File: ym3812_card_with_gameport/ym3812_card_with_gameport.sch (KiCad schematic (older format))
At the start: 79 parts, among them IC1 74LS138, IC11 NE558, IC12 74HCT02, IC13 74LS74, IC18 74LS244, IC2 74LS138, IC3 74LS138, IC4 74LS245, IC6 YM3812, IC7 Y3014B, IC8 LM324, IC9 TDA7233, J1 Bus_ISA_8bit

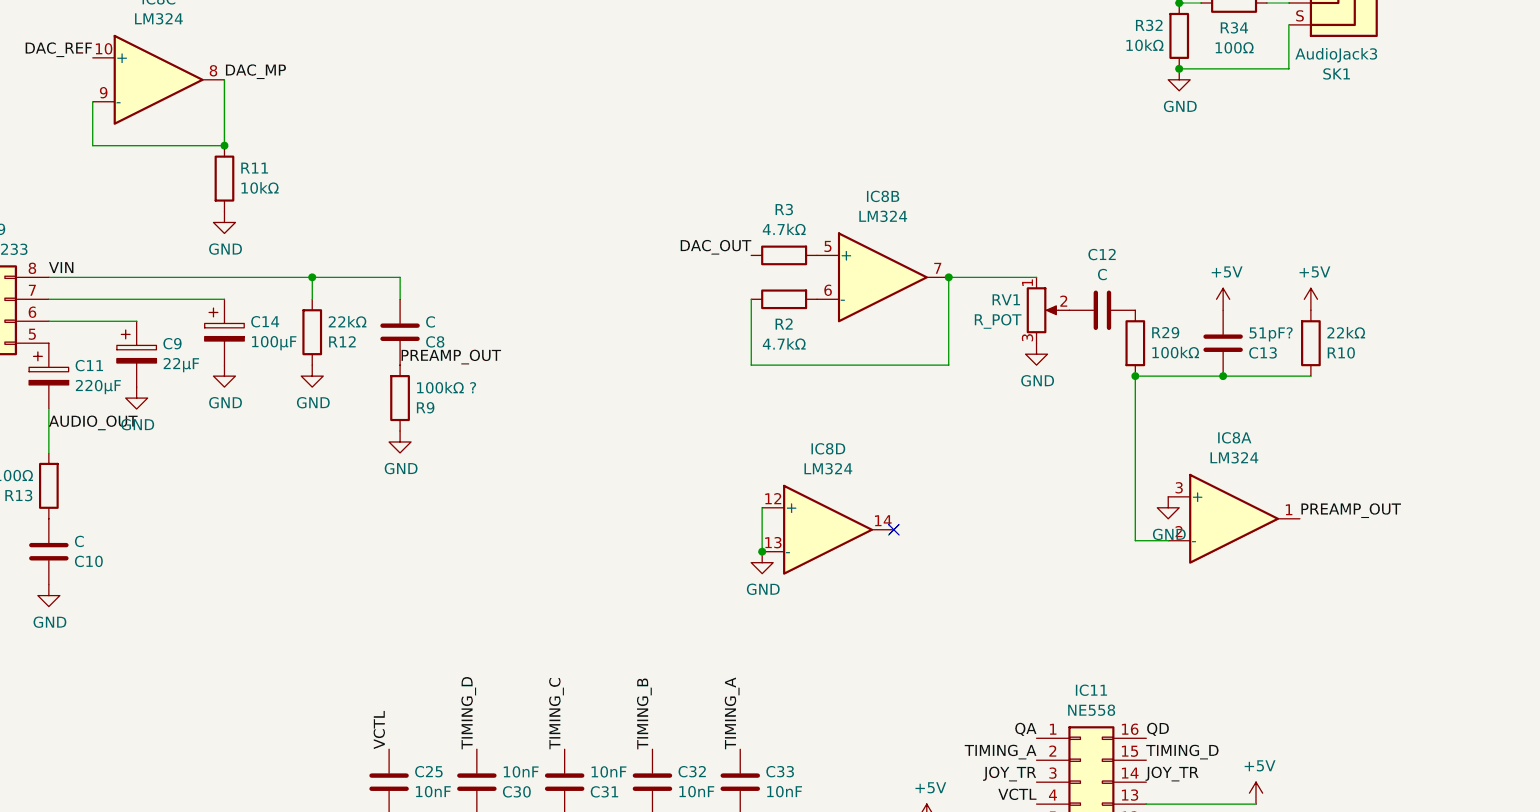
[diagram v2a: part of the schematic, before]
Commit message: corrections and some new traces
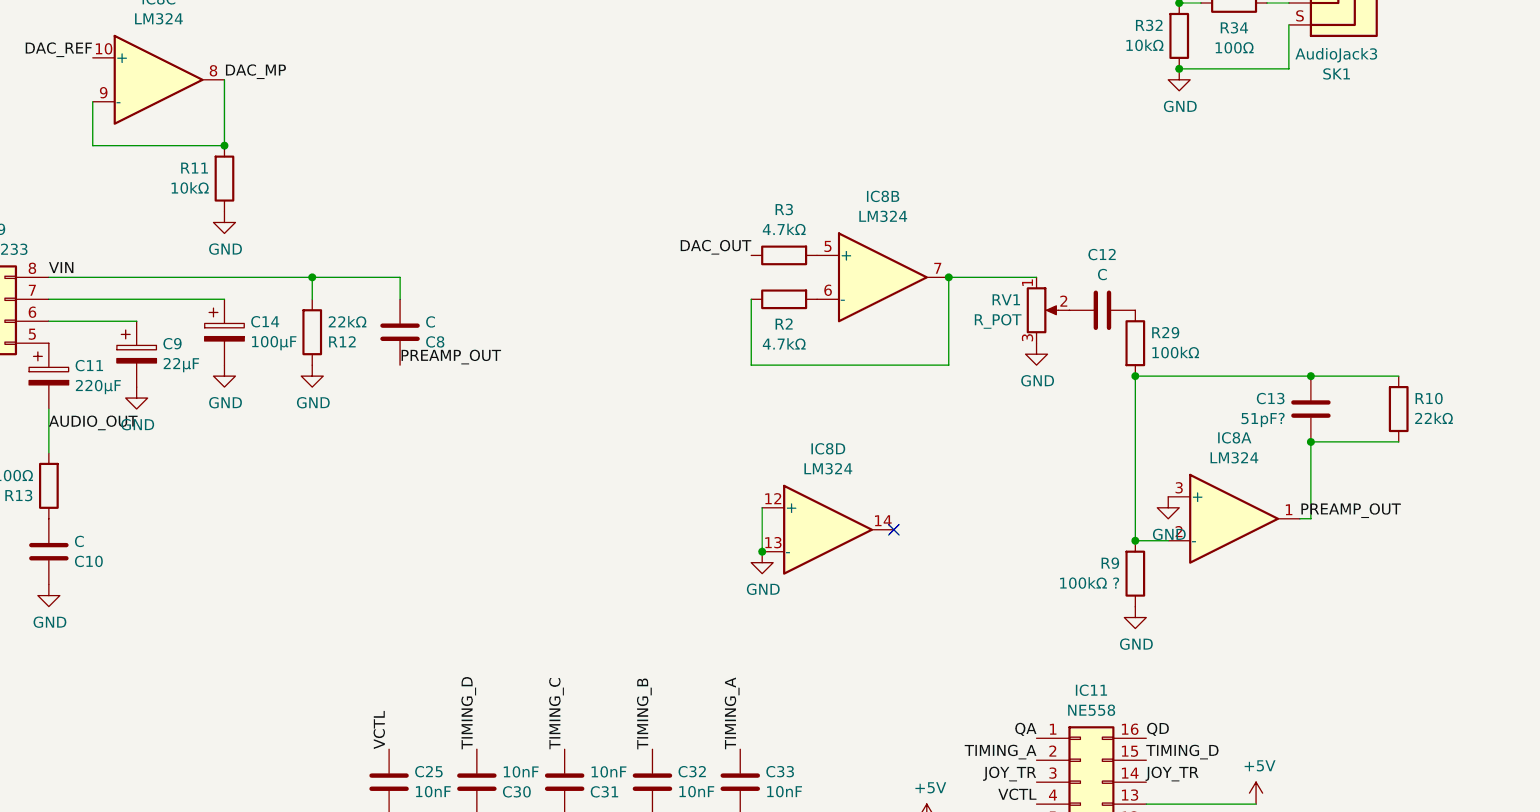
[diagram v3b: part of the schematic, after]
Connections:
- net +5V: no longer C13.2, R10.2
- net DAC_MP: now also R11.2; no longer R11.1
- net GND: now also R11.1; no longer R11.2
- net PREAMP_OUT: now also C13.1, R10.1; no longer R9.2
- net at IC8.2 (-), R29.2: now also C13.2, R10.2, R9.2; no longer C13.1, R10.1
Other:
- moved on the sheet: C13, R10, R9
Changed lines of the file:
@@
 EESchema Schematic File Version 4
-LIBS:ym3812_card_with_gameport-cache
 EELAYER 30 0
 EELAYER END
@@
 U 1 1 5D98CD88
 P 10200 2350
-F 0 "R11" H 10270 2396 50  0000 L CNN
-F 1 "10kΩ" H 10270 2305 50  0000 L CNN
+F 0 "R11" H 10131 2304 50  0000 R CNN
+F 1 "10kΩ" H 10131 2395 50  0000 R CNN
 F 2 "Resistor_SMD:R_1206_3216Metric" V 10130 2350 50  0001 C CNN
 F 3 "~" H 10200 2350 50  0001 C CNN
 	1    10200 2350
-	1    0    0    -1
+	1    0    0    1
 $EndComp
 $Comp
@@
 $EndComp
 $Comp
-L Device:R R10
-U 1 1 5D98D108
-P 15150 3100
-F 0 "R10" H 15220 3146 50  0000 L CNN
-F 1 "22kΩ" H 15220 3055 50  0000 L CNN
-F 2 "Resistor_SMD:R_1206_3216Metric" V 15080 3100 50  0001 C CNN
-F 3 "~" H 15150 3100 50  0001 C CNN
-	1    15150 3100
-	1    0    0    1
-$EndComp
-$Comp
 L Device:R R33
 U 1 1 5D98D9BF
@@
 L Device:R R9
 U 1 1 5D98DBBF
-P 11000 3350
-F 0 "R9" H 11070 3396 50  0000 L CNN
-F 1 "100kΩ ?" H 11070 3305 50  0000 L CNN
-F 2 "Resistor_SMD:R_1206_3216Metric" V 10930 3350 50  0001 C CNN
-F 3 "~" H 11000 3350 50  0001 C CNN
-	1    11000 3350
+P 14350 4150
+F 0 "R9" H 14281 4104 50  0000 R CNN
+F 1 "100kΩ ?" H 14281 4195 50  0000 R CNN
+F 2 "Resistor_SMD:R_1206_3216Metric" V 14280 4150 50  0001 C CNN
+F 3 "~" H 14350 4150 50  0001 C CNN
+	1    14350 4150
 	1    0    0    1
 $EndComp
@@
 $EndComp
 $Comp
-L Device:C C13
-U 1 1 5D9C6C30
-P 14750 3100
-F 0 "C13" H 14865 3146 50  0000 L CNN
-F 1 "51pF?" H 14865 3055 50  0000 L CNN
-F 2 "Capacitor_SMD:C_1206_3216Metric" H 14788 2950 50  0001 C CNN
-F 3 "~" H 14750 3100 50  0001 C CNN
-	1    14750 3100
-	1    0    0    1
-$EndComp
-$Comp
 L Device:C C34
 U 1 1 5D9C6E25
@@
 L power:GND #PWR0130
 U 1 1 5DB4EF8C
-P 11000 3500
-F 0 "#PWR0130" H 11000 3250 50  0001 C CNN
-F 1 "GND" H 11005 3327 50  0000 C CNN
-F 2 "" H 11000 3500 50  0001 C CNN
-F 3 "" H 11000 3500 50  0001 C CNN
-	1    11000 3500
+P 14350 4300
+F 0 "#PWR0130" H 14350 4050 50  0001 C CNN
+F 1 "GND" H 14355 4127 50  0000 C CNN
+F 2 "" H 14350 4300 50  0001 C CNN
+F 3 "" H 14350 4300 50  0001 C CNN
+	1    14350 4300
 	1    0    0    -1
 $EndComp
@@
 Text Label 15100 3900 0    50   ~ 0
 PREAMP_OUT
-Text Label 11000 3200 0    50   ~ 0
-PREAMP_OUT
 $Comp
 L power:+12V #PWR0133
@@
 F 3 "" H 800 10800 50  0001 C CNN
 	1    800  10800
-	1    0    0    -1
-$EndComp
-Wire Wire Line
-	14350 3250 14750 3250
-Connection ~ 14750 3250
-Wire Wire Line
-	14750 3250 15150 3250
-$Comp
-L power:+5V #PWR0180
-U 1 1 5DEDCA01
-P 15150 2950
-F 0 "#PWR0180" H 15150 2800 50  0001 C CNN
-F 1 "+5V" H 15165 3123 50  0000 C CNN
-F 2 "" H 15150 2950 50  0001 C CNN
-F 3 "" H 15150 2950 50  0001 C CNN
-	1    15150 2950
-	1    0    0    -1
-$EndComp
-$Comp
-L power:+5V #PWR0181
-U 1 1 5DEDD22B
-P 14750 2950
-F 0 "#PWR0181" H 14750 2800 50  0001 C CNN
-F 1 "+5V" H 14765 3123 50  0000 C CNN
-F 2 "" H 14750 2950 50  0001 C CNN
-F 3 "" H 14750 2950 50  0001 C CNN
-	1    14750 2950
 	1    0    0    -1
 $EndComp
@@
 	14500 4000 14350 4000
 Wire Wire Line
-	14350 4000 14350 3250
-Connection ~ 14350 3250
-Wire Wire Line
 	12650 4050 12650 3850
 Connection ~ 12650 4050
@@
 NoConn ~ 1000 3750
 $Comp
-L power:GND #PWR?
+L power:GND #PWR0154
 U 1 1 5E226AD7
 P 14500 3800
-F 0 "#PWR?" H 14500 3550 50  0001 C CNN
+F 0 "#PWR0154" H 14500 3550 50  0001 C CNN
 F 1 "GND" H 14505 3627 50  0000 C CNN
 F 2 "" H 14500 3800 50  0001 C CNN
@@
 NoConn ~ 14900 900
 NoConn ~ 14700 8800
+Connection ~ 14350 3250
+Wire Wire Line
+	14350 3250 15150 3250
+Wire Wire Line
+	15150 3250 15550 3250
+Connection ~ 15150 3250
+Wire Wire Line
+	15550 3550 15150 3550
+$Comp
+L Device:C C13
+U 1 1 5D9C6C30
+P 15150 3400
+F 0 "C13" H 15035 3354 50  0000 R CNN
+F 1 "51pF?" H 15035 3445 50  0000 R CNN
+F 2 "Capacitor_SMD:C_1206_3216Metric" H 15188 3250 50  0001 C CNN
+F 3 "~" H 15150 3400 50  0001 C CNN
+	1    15150 3400
+	1    0    0    1
+$EndComp
+$Comp
+L Device:R R10
+U 1 1 5D98D108
+P 15550 3400
+F 0 "R10" H 15620 3354 50  0000 L CNN
+F 1 "22kΩ" H 15620 3445 50  0000 L CNN
+F 2 "Resistor_SMD:R_1206_3216Metric" V 15480 3400 50  0001 C CNN
+F 3 "~" H 15550 3400 50  0001 C CNN
+	1    15550 3400
+	1    0    0    1
+$EndComp
+Wire Wire Line
+	15150 3550 15150 3900
+Wire Wire Line
+	15150 3900 15100 3900
+Connection ~ 15150 3550
+Wire Wire Line
+	14350 3250 14350 4000
+Text Label 11000 3200 0    50   ~ 0
+PREAMP_OUT
+Connection ~ 14350 4000
 $EndSCHEMATC

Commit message: minor corrections, routing complete
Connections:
- net +5V: now also IC2.6 (G1); no longer C7.1
- net BA01_NOR_BA02: no longer IC2.6 (G1)
- net DAC_REF: now also C7.1
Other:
- moved on the sheet: C7
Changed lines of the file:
@@
 L Device:CP C7
 U 1 1 5D92511A
-P 1400 10650
-F 0 "C7" H 1518 10696 50  0000 L CNN
-F 1 "10µF" H 1518 10605 50  0000 L CNN
-F 2 "Capacitor_THT:CP_Radial_D5.0mm_P2.50mm" H 1438 10500 50  0001 C CNN
-F 3 "~" H 1400 10650 50  0001 C CNN
-	1    1400 10650
+P 9200 1950
+F 0 "C7" H 9318 1996 50  0000 L CNN
+F 1 "10µF" H 9318 1905 50  0000 L CNN
+F 2 "Capacitor_THT:CP_Radial_D5.0mm_P2.50mm" H 9238 1800 50  0001 C CNN
+F 3 "~" H 9200 1950 50  0001 C CNN
+	1    9200 1950
 	1    0    0    -1
 $EndComp
@@
 Connection ~ 1000 10500
 Wire Wire Line
-	1000 10500 1400 10500
-Connection ~ 1400 10500
-Wire Wire Line
-	1400 10500 1800 10500
-Wire Wire Line
 	800  10800 1000 10800
 Connection ~ 1000 10800
-Wire Wire Line
-	1000 10800 1400 10800
-Connection ~ 1400 10800
-Wire Wire Line
-	1400 10800 1800 10800
 Wire Wire Line
 	5000 10500 4600 10500
@@
 Wire Wire Line
 	3000 6250 3000 6850
-Connection ~ 3000 6850
-Wire Wire Line
-	4800 6700 4800 6850
 Wire Wire Line
 	4500 6500 4500 6100
@@
 Wire Wire Line
 	4500 6500 4800 6500
-Wire Wire Line
-	3000 6850 4800 6850
 Text Label 4500 5900 0    50   ~ 0
 MAYBE_JOYSTICK
@@
 PREAMP_OUT
 Connection ~ 14350 4000
+$Comp
+L power:+5V #PWR?
+U 1 1 5DF4F747
+P 4500 6700
+F 0 "#PWR?" H 4500 6550 50  0001 C CNN
+F 1 "+5V" H 4515 6873 50  0000 C CNN
+F 2 "" H 4500 6700 50  0001 C CNN
+F 3 "" H 4500 6700 50  0001 C CNN
+	1    4500 6700
+	1    0    0    -1
+$EndComp
+Wire Wire Line
+	4500 6700 4800 6700
+Wire Wire Line
+	1000 10500 1800 10500
+Wire Wire Line
+	1000 10800 1800 10800
+Wire Wire Line
+	9200 1800 9600 1800
+$Comp
+L power:GND #PWR?
+U 1 1 5E013BD5
+P 9200 2100
+F 0 "#PWR?" H 9200 1850 50  0001 C CNN
+F 1 "GND" H 9205 1927 50  0000 C CNN
+F 2 "" H 9200 2100 50  0001 C CNN
+F 3 "" H 9200 2100 50  0001 C CNN
+	1    9200 2100
+	1    0    0    -1
+$EndComp
 $EndSCHEMATC

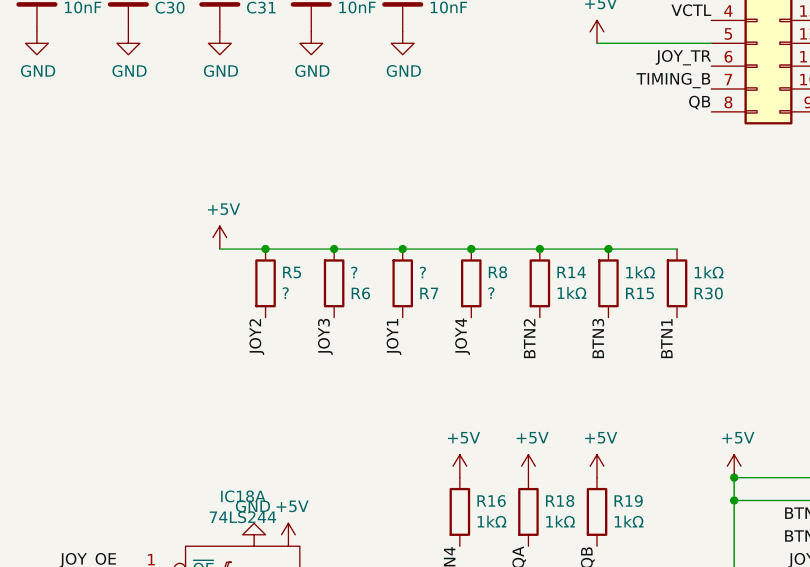
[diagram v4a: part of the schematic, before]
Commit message: mark R5, R6, R7 and R8 as DNP
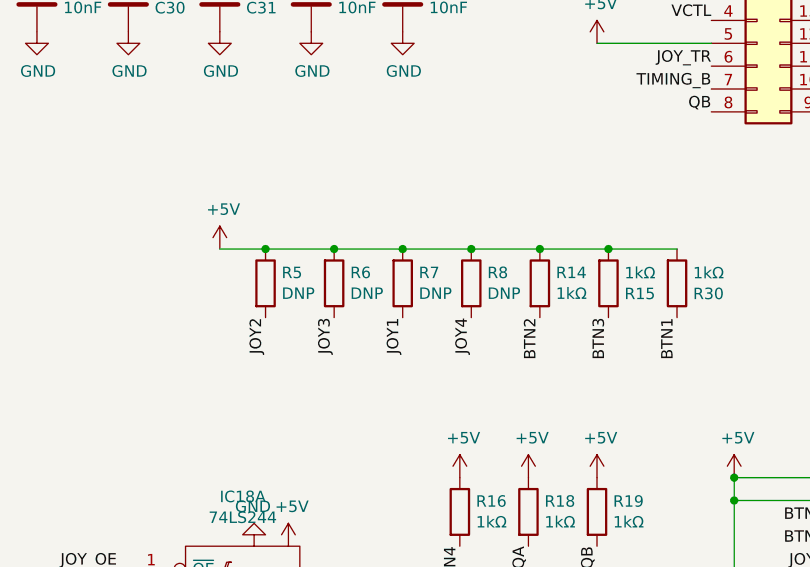
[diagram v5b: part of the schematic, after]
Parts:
- R5, R6, R7, R8: value ? -> DNP
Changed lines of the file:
@@
 P 11950 6350
 F 0 "R5" H 12020 6396 50  0000 L CNN
-F 1 "?" H 12020 6305 50  0000 L CNN
+F 1 "DNP" H 12020 6305 50  0000 L CNN
 F 2 "Resistor_SMD:R_1206_3216Metric" V 11880 6350 50  0001 C CNN
 F 3 "~" H 11950 6350 50  0001 C CNN
@@
 U 1 1 5D98D23A
 P 12250 6350
-F 0 "R6" H 12320 6396 50  0000 L CNN
-F 1 "?" H 12320 6305 50  0000 L CNN
+F 0 "R6" H 12320 6304 50  0000 L CNN
+F 1 "DNP" H 12320 6395 50  0000 L CNN
 F 2 "Resistor_SMD:R_1206_3216Metric" V 12180 6350 50  0001 C CNN
 F 3 "~" H 12250 6350 50  0001 C CNN
@@
 U 1 1 5D98D402
 P 12550 6350
-F 0 "R7" H 12620 6396 50  0000 L CNN
-F 1 "?" H 12620 6305 50  0000 L CNN
+F 0 "R7" H 12620 6304 50  0000 L CNN
+F 1 "DNP" H 12620 6395 50  0000 L CNN
 F 2 "Resistor_SMD:R_1206_3216Metric" V 12480 6350 50  0001 C CNN
 F 3 "~" H 12550 6350 50  0001 C CNN
@@
 P 12850 6350
 F 0 "R8" H 12920 6396 50  0000 L CNN
-F 1 "?" H 12920 6305 50  0000 L CNN
+F 1 "DNP" H 12920 6305 50  0000 L CNN
 F 2 "Resistor_SMD:R_1206_3216Metric" V 12780 6350 50  0001 C CNN
 F 3 "~" H 12850 6350 50  0001 C CNN
